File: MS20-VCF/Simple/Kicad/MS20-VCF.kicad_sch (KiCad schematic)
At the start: 57 parts, among them J5 Power Input, J6 FilterCV1, J7 FilterIn1, J8 FilterOut1, Q1 BC559, Q2 BC559, SW1 Hpass/Lpass Switch, U1 LM13700, U2 TL072

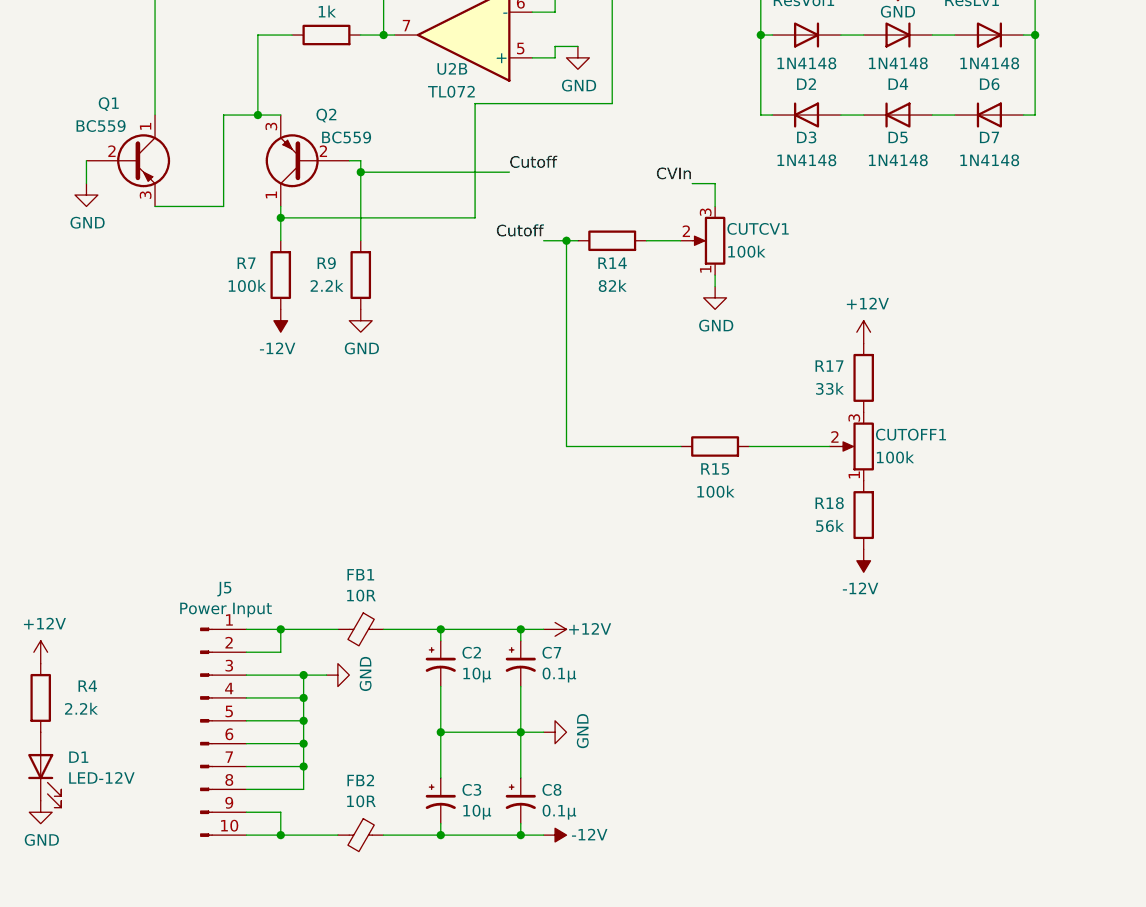
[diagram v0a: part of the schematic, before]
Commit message: MS20 VCF finished (no gerber files yet)
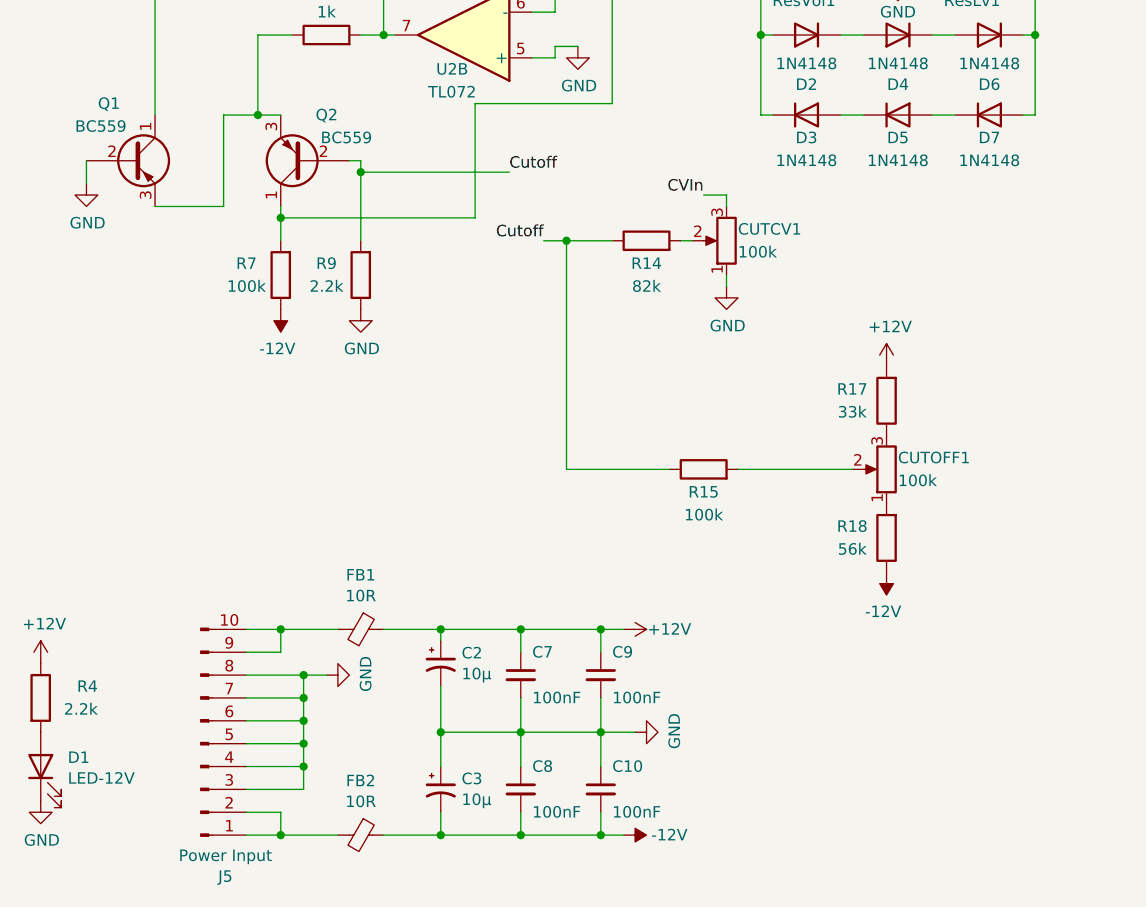
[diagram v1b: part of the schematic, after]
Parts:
- removed C7, C8: 0.1µ, Capacitor_THT:CP_Radial_D5.0mm_P2.00mm, symbol Device:CP1_Small
- added C10, C7, C8, C9: 100nF, Capacitor_THT:C_Disc_D7.0mm_W2.5mm_P5.00mm, symbol Device:C_Small
- CUTCV1, CUTOFF1, Res1: footprint Potentiometer_THT:Potentiometer_Bourns_PTV09A-1_Single_Vertical -> Synth:Pot-bourns-alpha
- J5: footprint Connector_PinHeader_2.54mm:PinHeader_2x05_P2.54mm_Vertical -> Connector_IDC:IDC-Header_2x05_P2.54mm_Vertical
- J6, J7, J8: footprint Connector_Audio:Jack_3.5mm_QingPu_WQP-PJ398SM_Vertical_CircularHoles -> Synth:Thonkiconn
- Q1, Q2: footprint Package_TO_SOT_THT:TO-92_Inline -> Package_TO_SOT_THT:TO-92_Inline_Wide
- U1: footprint Package_DIP:DIP-16_W7.62mm_Socket -> Package_SO:SOIC-16_3.9x9.9mm_P1.27mm
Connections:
- net +12V: now also C7.1, C9.1
- net -12V: now also C10.2, C8.2
- net GND: now also C10.1, C7.2, C8.1, C9.2
- net at J5.1 (Pin_1), J5.2 (Pin_2): now also FB2.2; no longer FB1.2
- net at J5.10 (Pin_10), J5.9 (Pin_9): now also FB1.2; no longer FB2.2
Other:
- moved on the sheet: C3, CUTCV1, CUTOFF1, R14, R15, R17, R18
